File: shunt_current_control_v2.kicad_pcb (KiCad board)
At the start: 4 copper layers, 97.5 x 100 mm, 116 parts, among them IC1 LT3042EMSE#PBF, IC2 LT3093EMSE#PBF, IC3 INA818IDR, IC4 TMUX6219DGKR, IC5 TLP116A_TPL,E, IC6 TLP116A_TPL,E, IC7 ADG1402BRMZ, IC8 ADP7118AUJZ-5.0-R7, J1 Conn_Coaxial, J10 Conn_Coaxial, J11 Conn_Coaxial, J12 Conn_Coaxial, J13 Conn_Coaxial, J14 Conn_Coaxial, J15 Conn_Coaxial, J16 Conn_Coaxial, J17 Conn_Coaxial, J2 7461057, J3 7461057, J4 7461057, J5 7461057, J6 Screw_Terminal_01x03, J7 Conn_Coaxial, J8 Conn_Coaxial, J9 Conn_Coaxial, Q1 2SC5242, Q2 2SC5242, Q3 2SD882, U1 INA592, U2 INA240A2D, U3 ADA4075-2, U5 OPA188xxDBV, U6 OPA188xxDBV

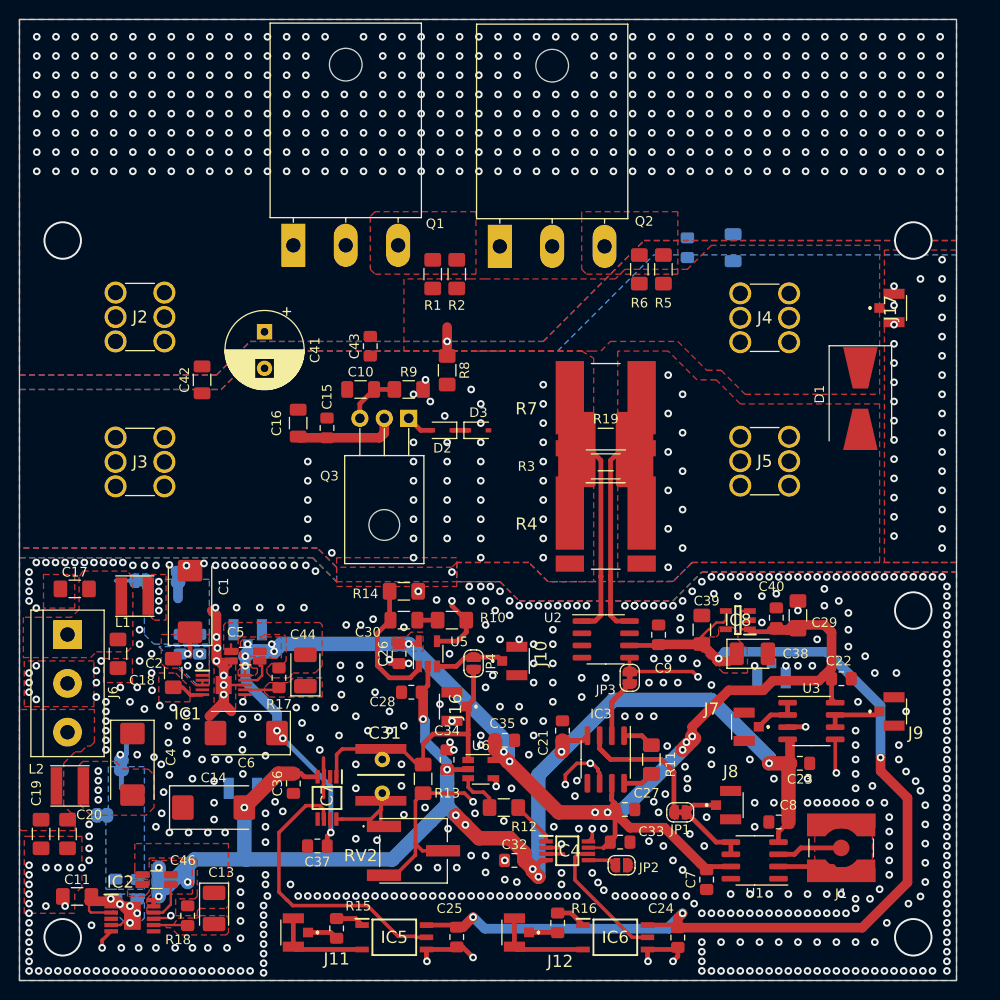
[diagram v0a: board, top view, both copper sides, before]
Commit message: Updated design, to include proper feedback and a current bias. Note the sign of the feedback might still be problematic. Need to be checked again
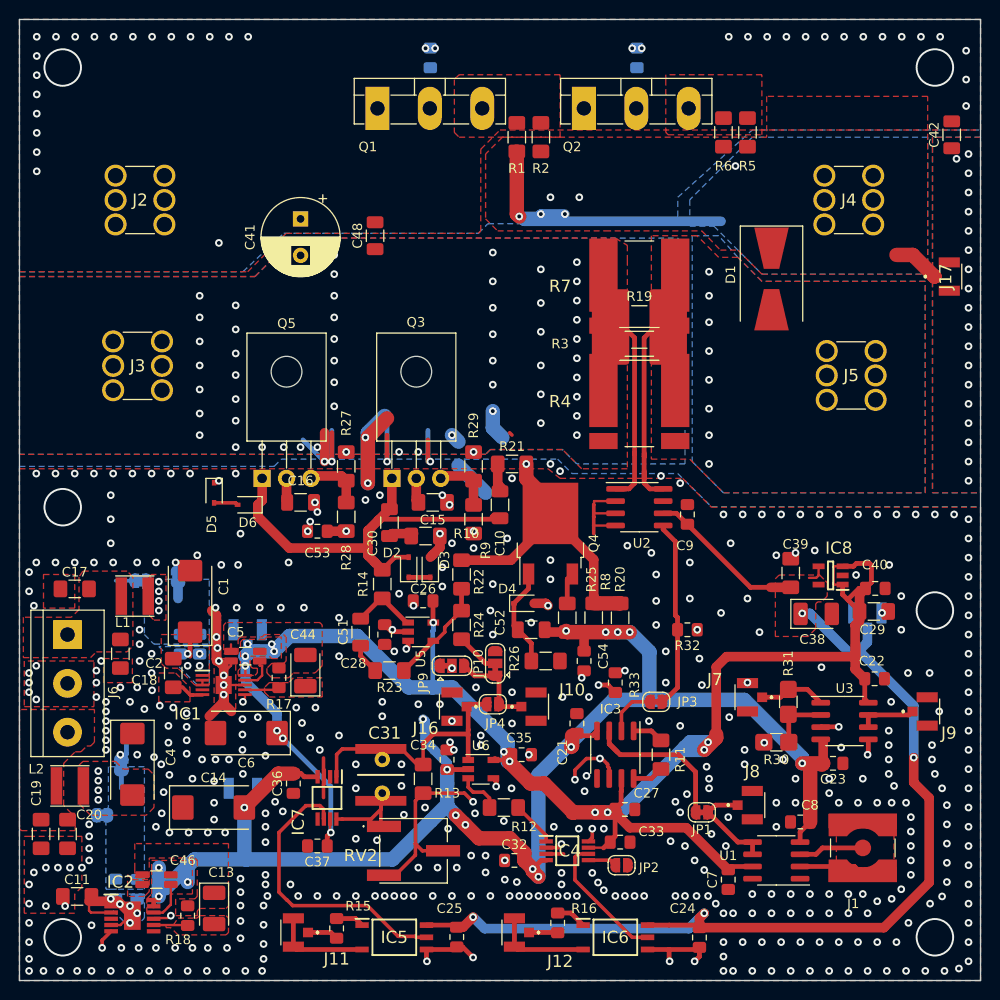
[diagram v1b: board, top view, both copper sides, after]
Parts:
- added C51: 1n, Capacitor_SMD:C_1206_3216Metric, F.Cu at (100.5, 99.8)
- added C52: 5n, Capacitor_SMD:C_1206_3216Metric, F.Cu at (118.2, 99.5)
- added C53: 0.1u, Capacitor_SMD:C_0805_2012Metric_Pad1.15x1.40mm_HandSolder, F.Cu at (96.0, 89.2)
- added C54: 0.1u, Capacitor_SMD:C_0805_2012Metric_Pad1.15x1.40mm_HandSolder, F.Cu at (123.8, 102.8)
- added D4: D3Z2V4BF-7, Diode_SMD:D_SOD-323, F.Cu at (117.5, 96.8)
- added D5: D, Diode_SMD:D_SOD-323, F.Cu at (85.2, 85.2)
- added D6: D3Z2V4BF-7, Diode_SMD:D_SOD-323, F.Cu at (88.8, 86.5)
- added JP10: SolderJumper_3_Bridged12, Jumper:SolderJumper-3_P1.3mm_Bridged12_RoundedPad1.0x1.5mm, F.Cu at (114.5, 103.0)
- added JP9: SolderJumper_3_Bridged12, Jumper:SolderJumper-3_P1.3mm_Bridged12_RoundedPad1.0x1.5mm, F.Cu at (110.0, 103.2)
- added Q4: 2scr573, Package_TO_SOT_SMD:TO-252-2, F.Cu at (120.2, 89.5)
- added Q5: 2SD882, Package_TO_SOT_THT:TO-126-3_Horizontal_TabDown, F.Cu at (90.2, 83.8)
- added R20: 5k, Resistor_SMD:R_1206_3216Metric_Pad1.42x1.75mm_HandSolder, F.Cu at (127.5, 98.2)
- added R21: 10, Resistor_SMD:R_1206_3216Metric_Pad1.42x1.75mm_HandSolder, F.Cu at (116.2, 82.2)
- added R22: 1000, Resistor_SMD:R_1206_3216Metric_Pad1.42x1.75mm_HandSolder, F.Cu at (111.0, 93.8)
- added R23: 1, Resistor_SMD:R_1206_3216Metric_Pad1.42x1.75mm_HandSolder, F.Cu at (103.5, 103.8)
- added R24: 330, Resistor_SMD:R_1206_3216Metric_Pad1.42x1.75mm_HandSolder, F.Cu at (111.0, 99.0)
- added R25: 200, Resistor_SMD:R_1206_3216Metric_Pad1.42x1.75mm_HandSolder, F.Cu at (122.0, 98.2)
- added R26: 5k, Resistor_SMD:R_1206_3216Metric_Pad1.42x1.75mm_HandSolder, F.Cu at (119.8, 102.8)
- added R27: 100m, Resistor_SMD:R_1206_3216Metric_Pad1.42x1.75mm_HandSolder, F.Cu at (99.0, 82.5)
- added R28: 5k, Resistor_SMD:R_1206_3216Metric_Pad1.42x1.75mm_HandSolder, F.Cu at (99.0, 87.8)
- added R29: 100m, Resistor_SMD:R_1206_3216Metric_Pad1.42x1.75mm_HandSolder, F.Cu at (112.2, 82.5)
- added R30: 500, SamacSys_Parts:R_1206_0805_dual, F.Cu at (143.8, 111.2)
- added R31: 500, SamacSys_Parts:R_1206_0805_dual, F.Cu at (145.0, 107.0)
- added R32: 50, Resistor_SMD:R_0805_2012Metric_Pad1.15x1.40mm_HandSolder, F.Cu at (134.5, 99.5)
- added R33: 50, Resistor_SMD:R_0805_2012Metric_Pad1.15x1.40mm_HandSolder, F.Cu at (127.0, 105.0)
- C10: value 0.1u -> 1n
- C15: value 0.1u -> 1u; footprint Capacitor_SMD:C_0805_2012Metric_Pad1.15x1.40mm_HandSolder -> Capacitor_SMD:C_1206_3216Metric_Pad1.42x1.75mm_HandSolder
- C30: value 0.1u -> 5n
- C43: moved to B.Cu
- C48: moved to F.Cu
- Q1, Q2: footprint Package_TO_SOT_THT:TO-3P-3_Horizontal_TabDown -> Package_TO_SOT_THT:TO-3P-3_Vertical
- R10: value 1 -> 10
- R14: value 50 -> 10
- R8, R9: value 2k -> 5k
- moved C42 82.1 mm to (162.0, 48.0)
- moved C48 37.3 mm to (102.0, 58.5)
- moved C43 30.6 mm to (107.8, 40.0), turned to 270 degrees
- moved R8 29.9 mm to (124.8, 98.2)
- moved C49 20.4 mm to (129.2, 40.0), turned to 270 degrees
- moved C10 18.8 mm to (115.0, 86.5), turned to 270 degrees
- moved Q2 16.8 mm to (123.7, 45.2)
- moved Q1 16.7 mm to (102.2, 45.2)
- moved R1 16.7 mm to (116.8, 48.2)
- moved R2 16.7 mm to (119.2, 48.2)
- moved R5 16.7 mm to (140.8, 47.8)
- moved R6 16.7 mm to (138.2, 47.8)
- moved D1 15.5 mm to (143.2, 63.0)
- moved D3 15.1 mm to (107.8, 93.0), turned to 90 degrees
- moved R9 15.1 mm to (112.2, 88.0), turned to 270 degrees
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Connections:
- C10 pad 1: GNDA -> Net-(C10-Pad1)
- C10 pad 2: /drive_and_measure/Darlington -> /drive_and_measure/BJT_drive
- C30 pad 2: Net-(C30-Pad2) -> /drive_and_measure/BJT_drive
- D1 pad 1: /drive_and_measure/Coil_P -> Net-(D1-Pad1)
- J17 pad 1: /drive_and_measure/Coil_P -> Net-(D1-Pad1)
- J4 pad 1: /drive_and_measure/Coil_P -> Net-(D1-Pad1)
- J4 pad 2: /drive_and_measure/Coil_P -> Net-(D1-Pad1)
- J4 pad 3: /drive_and_measure/Coil_P -> Net-(D1-Pad1)
- J4 pad 4: /drive_and_measure/Coil_P -> Net-(D1-Pad1)
- J4 pad 5: /drive_and_measure/Coil_P -> Net-(D1-Pad1)
- J4 pad 6: /drive_and_measure/Coil_P -> Net-(D1-Pad1)
- J7 pad 1: Net-(J7-Pad1) -> CurrentSense2X
- Q3 pad 3: /drive_and_measure/Darlington -> Net-(Q3-Pad3)
- R1 pad 2: /drive_and_measure/Coil_P -> Net-(D1-Pad1)
- R10 pad 2: /drive_and_measure/Coil_P -> GNDA
- R14 pad 2: Net-(C30-Pad2) -> Net-(C51-Pad2)
- R2 pad 2: /drive_and_measure/Coil_P -> Net-(D1-Pad1)
- R5 pad 2: /drive_and_measure/Coil_P -> Net-(D1-Pad1)
- R6 pad 2: /drive_and_measure/Coil_P -> Net-(D1-Pad1)
- R8 pad 1: /drive_and_measure/Coil_P -> Net-(D1-Pad1)
- R8 pad 2: GNDA -> -12VA
- R9 pad 1: /drive_and_measure/Darlington -> Net-(Q3-Pad3)
- R9 pad 2: GNDA -> -12VA
- U3 pad 1: Net-(J7-Pad1) -> CurrentSense2X
- U3 pad 2: Net-(J7-Pad1) -> Net-(R30-Pad1)
- U3 pad 3: CurrentSense -> Net-(R32-Pad1)
- U3 pad 5: Error -> Net-(R33-Pad1)
- U5 pad 1: Net-(C30-Pad2) -> Net-(C51-Pad2)
- U5 pad 3: CoilVoltage -> Net-(JP9-Pad2)
- U5 pad 4: /drive_and_measure/Coil_P -> Net-(R22-Pad2)
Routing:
- net Net-(D1-Pad1): track 0.00 -> 97.5 mm, vias 0 -> 7
- net -12VA: track 144.5 -> 225.6 mm, vias 12 -> 20
- net GNDA: track 78.6 -> 141.7 mm, vias 629 -> 520
- net /drive_and_measure/Coil_P: track 39.6 -> 0.00 mm, vias 2 -> 0
- net Net-(R33-Pad1): track 0.00 -> 31.9 mm, vias 0 -> 2
- net +5VP: track 0.00 -> 25.1 mm, vias 371 -> 36
- net Error: track 50.2 -> 25.8 mm
- net +12VA: track 159.2 -> 182.7 mm, vias 16 -> 15
- net /drive_and_measure/BJT_drive: track 23.5 -> 44.9 mm, vias 1 -> 0
- net Net-(R32-Pad1): track 0.00 -> 20.8 mm, vias 0 -> 2
- net Net-(C30-Pad2): track 13.8 -> 0.00 mm
- net /drive_and_measure/Darlington: track 5.73 -> 18.4 mm, vias 0 -> 2
- net Net-(R22-Pad2): track 0.00 -> 11.2 mm
- net Net-(C52-Pad2): track 0.00 -> 10.4 mm
- net CurrentSense2X: track 0.00 -> 7.02 mm
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- added copper zone on B.Cu, net /drive_and_measure/Coil_N
- added copper zone on B.Cu, net Net-(D1-Pad1)
- added copper zone on F.Cu, net Net-(D1-Pad1)
- added copper zone on In2.Cu, net Net-(D1-Pad1)
- removed copper zone on In1.Cu, net +5VP
- removed copper zone on F.Cu, net /drive_and_measure/Coil_P
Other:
- board size 97.5 x 100 mm -> 100 x 100 mm

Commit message: Allowed swapping feedback signs
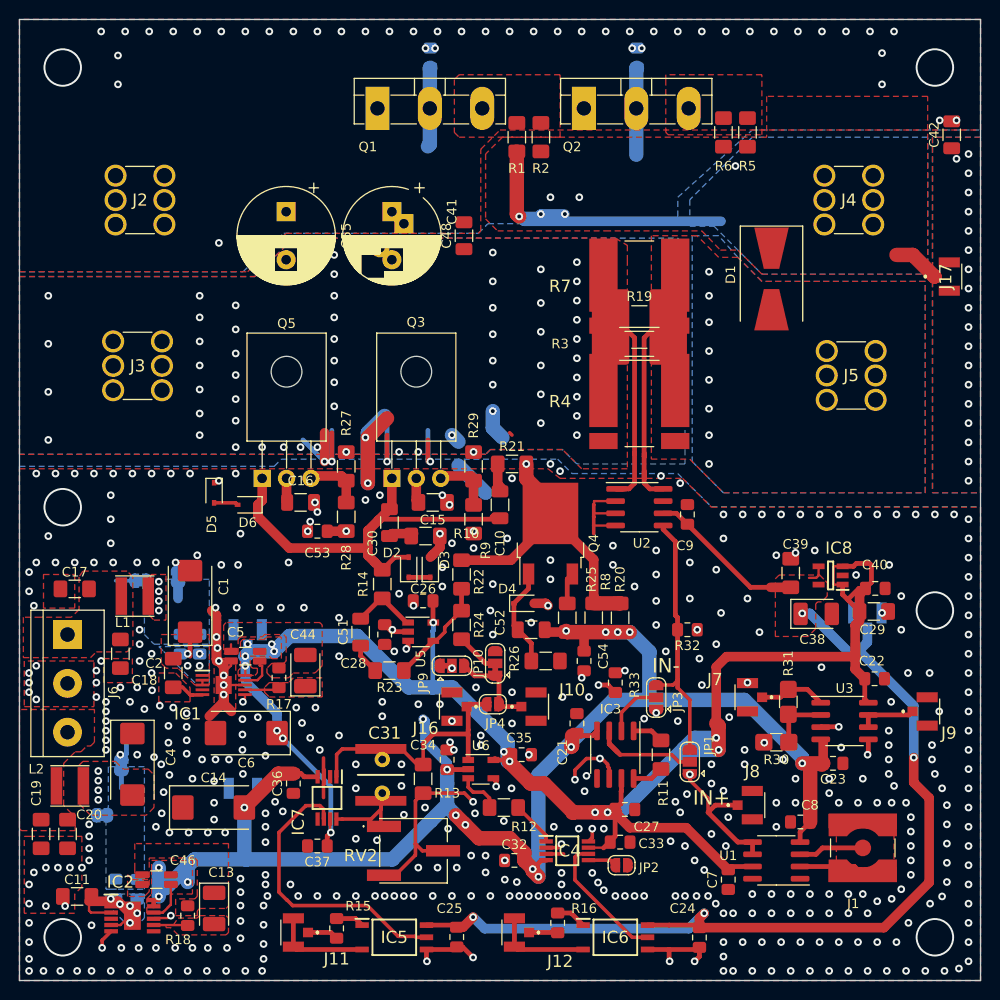
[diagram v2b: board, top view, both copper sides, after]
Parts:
- added C55: 2000uF, Capacitor_THT:CP_Radial_D10.0mm_P5.00mm, F.Cu at (92.8, 56.0)
- C41: footprint Capacitor_THT:CP_Radial_D8.0mm_P3.80mm -> SamacSys_Parts:CP_Radial_D10.0mm_P3.5_5
- JP1, JP3: value Jumper -> SolderJumper_3_Open; footprint Jumper:SolderJumper-2_P1.3mm_Bridged_RoundedPad1.0x1.5mm -> Jumper:SolderJumper-3_P1.3mm_Open_RoundedPad1.0x1.5mm
- moved C41 9.53 mm to (103.8, 56.0)
- moved C48 9.25 mm to (111.2, 58.5)
- moved JP1 5.40 mm to (134.8, 113.2), turned to 90 degrees
- moved JP3 0.45 mm to (131.2, 106.5), turned to 90 degrees
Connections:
- net Net-(D1-Pad1) renamed /drive_and_measure/Coil_P
- JP3 pad 1: Net-(IC3-Pad2) -> SetPoint
- JP3 pad 2: CurrentSense -> Net-(IC3-Pad2)
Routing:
- net +5VP: track 25.1 -> 46.9 mm, vias 36 -> 25
- net SetPoint: track 10.6 -> 23.1 mm, vias 0 -> 2
- net CurrentSense: track 20.1 -> 26.9 mm
- net Net-(IC3-Pad3): track 17.0 -> 11.8 mm
- net +12VA: track 182.7 -> 186.0 mm
- net Net-(IC3-Pad2): track 5.34 -> 6.17 mm
- net GNDA: vias 520 -> 545
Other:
- board text added: "IN+"
- board text added: "IN-"

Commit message: Relay array board; Last checkup; Gerberfile updates
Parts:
- added D7: D, Diode_SMD:D_SOD-323_HandSoldering, F.Cu at (90.0, 114.2)
- added D8: D, Diode_SMD:D_SOD-323_HandSoldering, F.Cu at (95.5, 109.2)
- D2, D3, D4, D5, D6: footprint Diode_SMD:D_SOD-323 -> Diode_SMD:D_SOD-323_HandSoldering
- moved IC6 1.00 mm to (128.0, 131.5)
- moved J12 0.60 mm to (117.1, 131.0)
- moved R16 0.60 mm to (121.6, 130.0)
- moved C24 0.25 mm to (135.5, 131.5)
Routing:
- net +12VA: track 186.0 -> 188.9 mm, vias 15 -> 16
- net Net-(IC6-Pad3): track 10.2 -> 11.6 mm
- net ^FeedbackEngage: track 13.9 -> 14.9 mm
- net GNDA: track 141.7 -> 140.7 mm
- net +5VA: track 121.4 -> 120.4 mm
